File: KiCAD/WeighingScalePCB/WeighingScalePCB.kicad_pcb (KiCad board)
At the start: 2 copper layers, 94.6 x 73.3 mm, 79 parts, among them IC1 MAX6675ISA+T, IC2 APS11753KMDALX-9PL5, J1 Conn_01x14_MountingPin, J2 AudioJack4, J4 Battery Conn, J6 Conn_01x04_MountingPin, Q2 NX138AKR, Q3 NX138AKR, Q4 NX138AKR, Q5 NX138AKR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

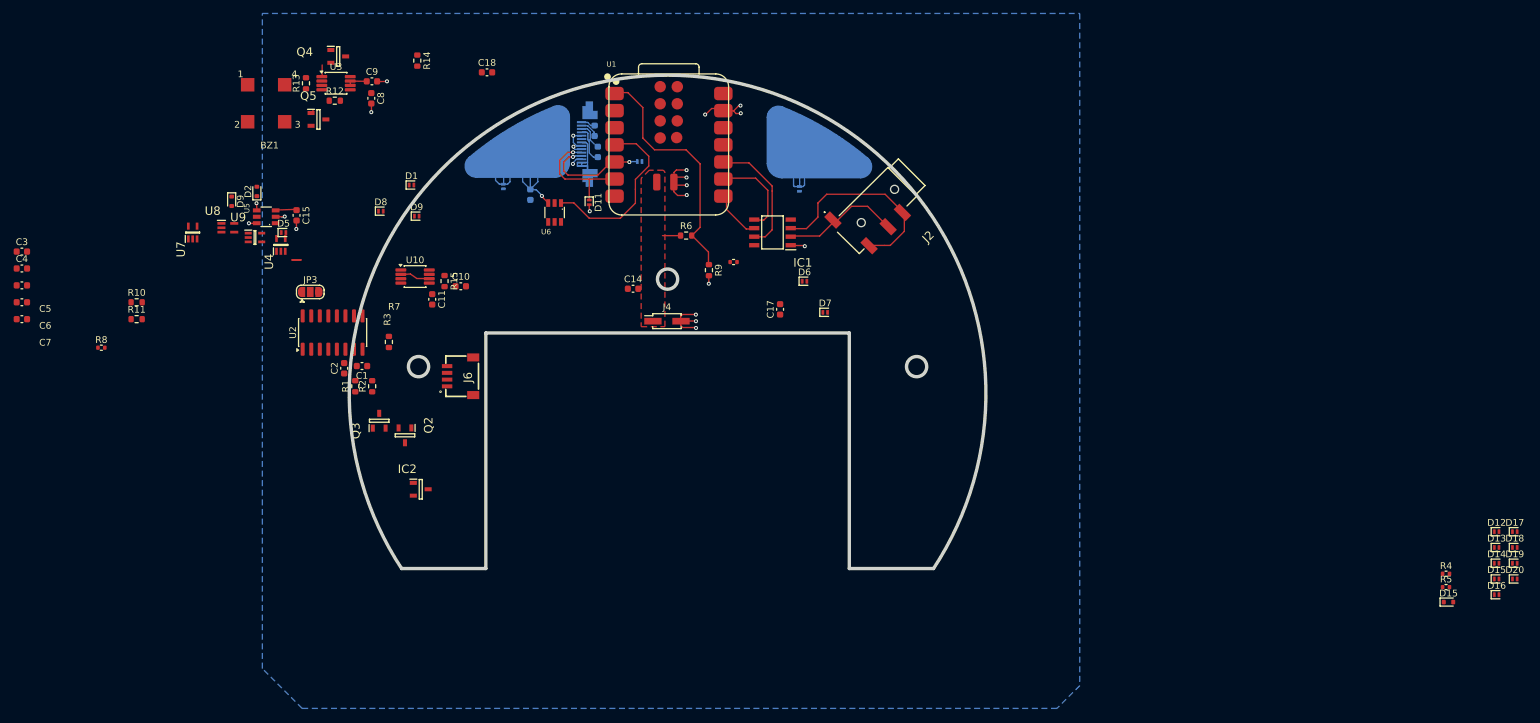
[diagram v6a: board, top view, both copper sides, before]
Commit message: layout done, decap placement and ferrite bead choice pending
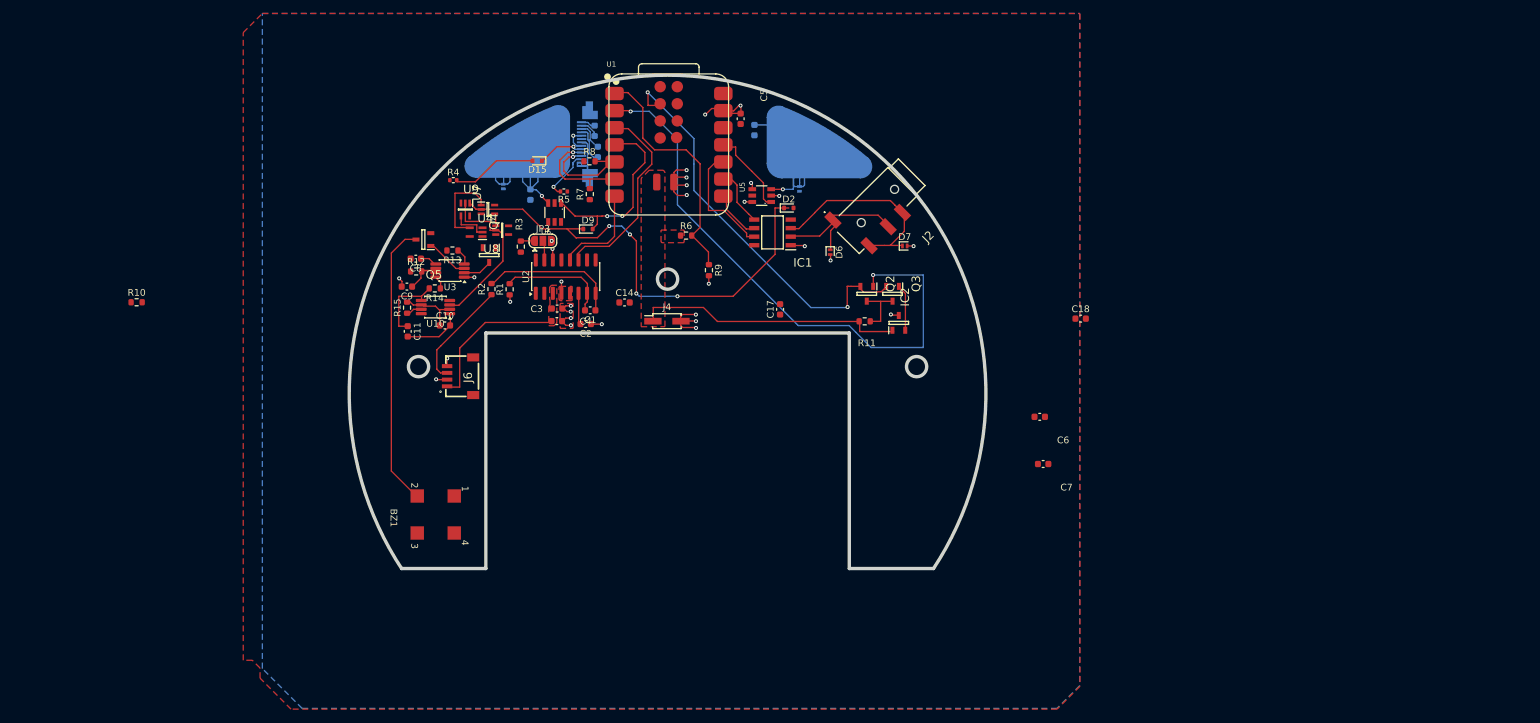
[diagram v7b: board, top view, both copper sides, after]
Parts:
- removed D1, D10, D11, D12, D13, D14, D16, D17, D18, D19, D20, D5, D8: PESD3V3U1UL, Diode_SMD:D_SOD-882
- removed the D15 at (270.1, 111.6)
- removed the D9 at (109.6, 57.7)
- C15: moved to B.Cu
- R7, R8: footprint Resistor_SMD:R_0402_1005Metric -> Resistor_SMD:R_0603_1608Metric
- moved R4 158.7 mm to (115.0, 52.4)
- moved C7 153.3 mm to (202.7, 94.5)
- moved C6 152.2 mm to (202.2, 87.5)
- moved D15 150.4 mm to (127.5, 49.5), turned to 180 degrees
- moved R5 143.6 mm to (131.5, 54.0), turned to 180 degrees
- moved C5 109.6 mm to (157.7, 43.2), turned to 90 degrees
- moved R11 108.2 mm to (176.2, 73.3)
- moved C18 95.5 mm to (208.3, 72.9)
- moved C3 80.0 mm to (130.5, 71.4), turned to 180 degrees
- moved C4 79.9 mm to (130.4, 73.3), turned to 180 degrees
- moved D2 79.1 mm to (164.9, 56.5), turned to 0 degrees
- moved Q3 78.6 mm to (180.3, 69.2), turned to -90 degrees
- moved R8 77.6 mm to (135.3, 49.6)
- moved IC2 75.2 mm to (181.2, 73.6), turned to 90 degrees
- moved U5 73.7 mm to (160.9, 54.7)
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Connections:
- net Net-(D5-K) renamed /buzz_drive
- net Net-(Q4-D) renamed /buzz_pull_down
- JP3 pad 2: GND -> Net-(JP3-C)
- JP3 pad 3: Net-(JP3-B) -> GND
- U1 pad 11: PD_SCK -> Tare
- U1 pad 3: Tare -> PD_SCK
- U2 pad 15: Net-(JP3-B) -> Net-(JP3-C)
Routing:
- net Time: vias 0 -> 2
- net SDA: vias 2 -> 1
- net GND: vias 19 -> 30
- net /touch1: vias 0 -> 1
- net /timeORtare: vias 0 -> 4
- net /enable: vias 0 -> 2
- net /ble_keep_awake: vias 0 -> 2
- added copper zone on F.Cu, net /DVDD_ldcell
- added copper zone on F.Cu, net GND
- added copper zone on F.Cu, net VCC

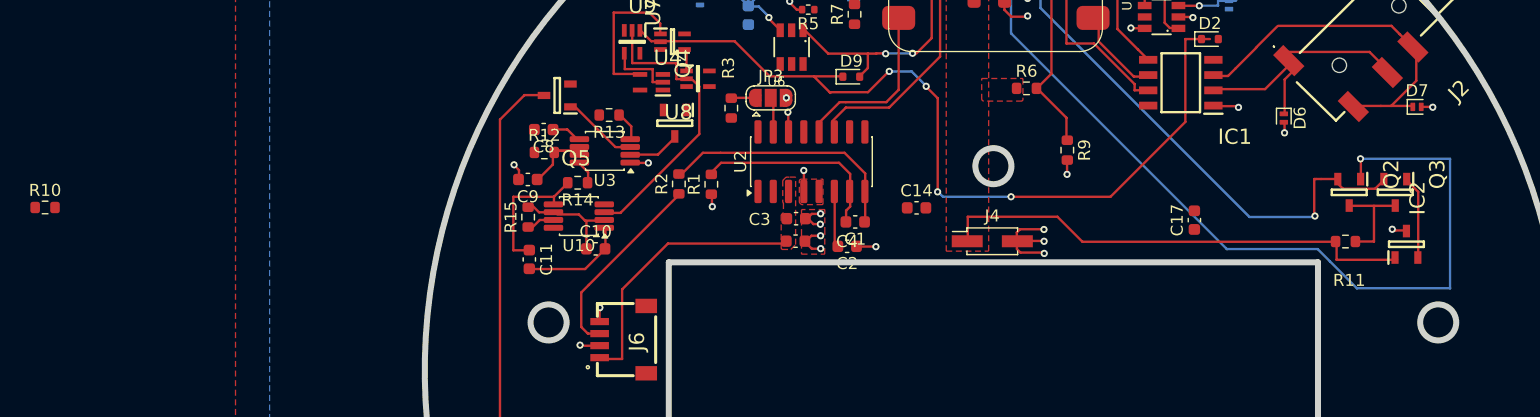
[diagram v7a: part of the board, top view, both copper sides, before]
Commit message: dvdd for loadcell updated as a pwr pour
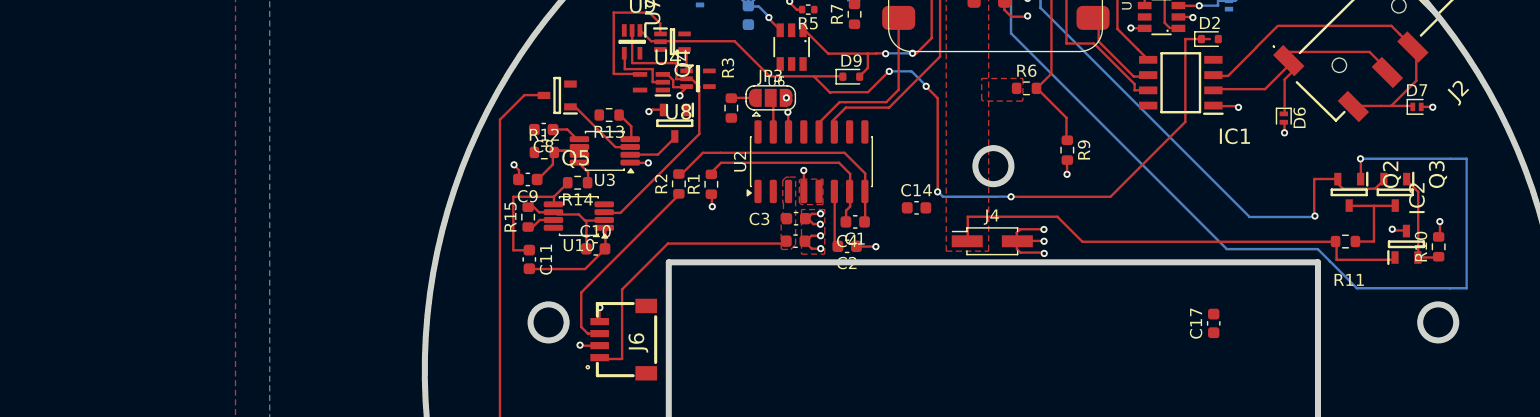
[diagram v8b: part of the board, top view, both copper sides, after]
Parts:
- moved R10 116.0 mm to (183.9, 73.8), turned to 90 degrees
- moved C17 8.74 mm to (165.2, 80.2)
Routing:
- net GND: vias 30 -> 33
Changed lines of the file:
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@@
 	(footprint "Capacitor_SMD:C_0603_1608Metric"
 		(layer "F.Cu")
-		(at 163.6 71.56 90)
+		(at 165.21 80.15 90)
 		(descr "Capacitor SMD 0603 (1608 Metric), square (rectangular) end terminal, IPC-7351 nominal, (Body size source: IPC-SM-782 page 76, https://www.pcb-3d.com/wordpress/wp-content/uploads/ipc-sm-782a_amendment_1_and_2.pdf), generated with kicad-footprint-generator")
 		(tags "capacitor")
@@
 	(footprint "Resistor_SMD:R_0603_1608Metric"
 		(layer "F.Cu")
-		(at 68 70.51)
+		(at 183.92 73.78 90)
 		(descr "Resistor SMD 0603 (1608 Metric), square (rectangular) end terminal, IPC-7351 nominal, (Body size source: IPC-SM-782 page 72, https://www.pcb-3d.com/wordpress/wp-content/uploads/ipc-sm-782a_amendment_1_and_2.pdf), generated with kicad-footprint-generator")
 		(tags "resistor")
 		(property "Reference" "R10"
-			(at 0 -1.43 0)
+			(at 0 -1.43 90)
 			(layer "F.SilkS")
 			(effects
@@
 		)
 		(property "Value" "1K"
-			(at 0 1.43 0)
+			(at 0 1.43 90)
 			(layer "F.Fab")
 			(effects
@@
 		)
 		(property "Datasheet" "~"
-			(at 0 0 0)
+			(at 0 0 90)
 			(layer "F.Fab")
 			(hide yes)
@@
 		)
 		(property "Description" "Resistor, US symbol"
-			(at 0 0 0)
+			(at 0 0 90)
 			(layer "F.Fab")
 			(hide yes)
@@
 		)
 		(fp_line
-			(start -1.48 -0.73)
-			(end 1.48 -0.73)
+			(start 1.48 -0.73)
+			(end 1.48 0.73)
 			(stroke
 				(width 0.05)
@@
 		)
 		(fp_line
-			(start -1.48 0.73)
-			(end -1.48 -0.73)
+			(start -1.48 -0.73)
+			(end 1.48 -0.73)
 			(stroke
 				(width 0.05)
@@
 		)
 		(fp_line
-			(start 1.48 -0.73)
-			(end 1.48 0.73)
+			(start 1.48 0.73)
+			(end -1.48 0.73)
 			(stroke
 				(width 0.05)
@@
 		)
 		(fp_line
-			(start 1.48 0.73)
-			(end -1.48 0.73)
+			(start -1.48 0.73)
+			(end -1.48 -0.73)
 			(stroke
 				(width 0.05)
@@
 		)
 		(fp_line
-			(start -0.8 -0.4125)
-			(end 0.8 -0.4125)
+			(start 0.8 -0.4125)
+			(end 0.8 0.4125)
 			(stroke
 				(width 0.1)
@@
 		)
 		(fp_line
-			(start -0.8 0.4125)
-			(end -0.8 -0.4125)
+			(start -0.8 -0.4125)
+			(end 0.8 -0.4125)
 			(stroke
 				(width 0.1)
@@
 		)
 		(fp_line
-			(start 0.8 -0.4125)
-			(end 0.8 0.4125)
+			(start 0.8 0.4125)
+			(end -0.8 0.4125)
 			(stroke
 				(width 0.1)
@@
 		)
 		(fp_line
-			(start 0.8 0.4125)
-			(end -0.8 0.4125)
+			(start -0.8 0.4125)
+			(end -0.8 -0.4125)
 			(stroke
 				(width 0.1)
@@
 		)
 		(fp_text user "${REFERENCE}"
-			(at 0 0 0)
+			(at 0 0 90)
 			(layer "F.Fab")
 			(effects
@@
 		)
 		(pad "1" smd roundrect
-			(at -0.825 0)
+			(at -0.825 0 90)
 			(size 0.8 0.95)
 			(layers "F.Cu" "F.Mask" "F.Paste")
@@
 		)
 		(pad "2" smd roundrect
-			(at 0.825 0)
+			(at 0.825 0 90)
 			(size 0.8 0.95)
 			(layers "F.Cu" "F.Mask" "F.Paste")
@@
 	)
 	(gr_line
+		(start 119.44 62.37)
+		(end 118.53 62.37)
+		(stroke
+			(width 0.2)
+			(type default)
+		)
+		(layer "F.Cu")
+		(net 10)
+	)
+	(gr_line
 		(start 168.725 57.215)
 		(end 170.495 55.445)
@@
 	)
 	(gr_line
+		(start 121.37 60.5)
+		(end 120.25 60.5)
+		(stroke
+			(width 0.2)
+			(type default)
+		)
+		(layer "F.Cu")
+		(net 10)
+	)
+	(gr_line
 		(start 152.96 56.87)
 		(end 152.96 50.74)
@@
 	)
 	(gr_line
+		(start 118.53 62.37)
+		(end 118.24 62.66)
+		(stroke
+			(width 0.2)
+			(type default)
+		)
+		(layer "F.Cu")
+		(net 10)
+	)
+	(gr_line
 		(start 151.71 59.38)
 		(end 151.71 49.94)
@@
 	)
 	(gr_line
+		(start 120.25 60.5)
+		(end 120.25 59.92)
+		(stroke
+			(width 0.2)
+			(type default)
+		)
+		(layer "F.Cu")
+		(net 10)
+	)
+	(gr_line
 		(start 139.14 44.71)
 		(end 141.04 44.71)
@@
 	)
 	(gr_line
+		(start 183.96 74.67)
+		(end 182.27 74.67)
+		(stroke
+			(width 0.2)
+			(type default)
+		)
+		(layer "F.Cu")
+		(net 22)
+	)
+	(gr_line
 		(start 118.33 52.61)
 		(end 115.62 52.61)
@@
 	)
 	(gr_line
+		(start 184.03 72.83)
+		(end 184.03 71.69)
+		(stroke
+			(width 0.2)
+			(type default)
+		)
+		(layer "F.Cu")
+		(net 10)
+	)
+	(gr_line
 		(start 107.42 67.4)
 		(end 107.05 67.03)
@@
 	)
 	(gr_line
+		(start 120.25 59.92)
+		(end 119.68 59.35)
+		(stroke
+			(width 0.2)
+			(type default)
+		)
+		(layer "F.Cu")
+		(net 10)
+	)
+	(gr_line
 		(start 115.3 54.3)
 		(end 115.3 59.4)
@@
 	)
 	(gr_line
+		(start 121.37 60.5)
+		(end 120.73 61.14)
+		(stroke
+			(width 0.2)
+			(type default)
+		)
+		(layer "F.Cu")
+		(net 10)
+	)
+	(gr_line
 		(start 142.23 46.96)
 		(end 139.75 46.96)
@@
 	)
 	(gr_line
-		(start 184.87 77.23)
-		(end 184.87 66.46)
+		(start 186.25 77.225)
+		(end 186.25 66.455)
 		(stroke
 			(width 0.2)
@@
 	)
 	(gr_line
+		(start 186.25 66.455)
+		(end 184.87 66.455)
+		(stroke
+			(width 0.2)
+			(type default)
+		)
+		(layer "B.Cu")
+		(net 48)
+	)
+	(gr_line
 		(start 135.02 44.28)
 		(end 136 45.26)
@@
 	)
 	(gr_line
+		(start 184.87 77.23)
+		(end 186.25 77.23)
+		(stroke
+			(width 0.2)
+			(type default)
+		)
+		(layer "B.Cu")
+		(net 48)
+	)
+	(gr_line
 		(start 132.97 47.64)
 		(end 132.97 47.42)
@@
 	)
 	(via
+		(at 118.23 62.53)
+		(size 0.6)
+		(drill 0.3)
+		(layers "F.Cu" "B.Cu")
+		(free yes)
+		(net 10)
+	)
+	(via
 		(at 129.66 61.39)
 		(size 0.6)
@@
 	)
 	(via
+		(at 120.81 61.22)
+		(size 0.6)
+		(drill 0.3)
+		(layers "F.Cu" "B.Cu")
+		(free yes)
+		(net 10)
+	)
+	(via
 		(at 151.11 74.33)
 		(size 0.6)
@@
 	)
 	(via
+		(at 184.02 71.68)
+		(size 0.6)
+		(drill 0.3)
+		(layers "F.Cu" "B.Cu")
+		(free yes)
+		(net 10)
+	)
+	(via
 		(at 158.32 55.58)
 		(size 0.6)
@@
 		(layer "F.Cu")
 		(hatch edge 0.5)
-		(priority 1)
+		(priority 7)
 		(connect_pads
 			(clearance 0.5)
